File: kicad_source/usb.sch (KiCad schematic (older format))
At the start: 19 parts, among them P1 USB_OTG, Q3 BC847, Q4 BC847, U4 CP2102N_28

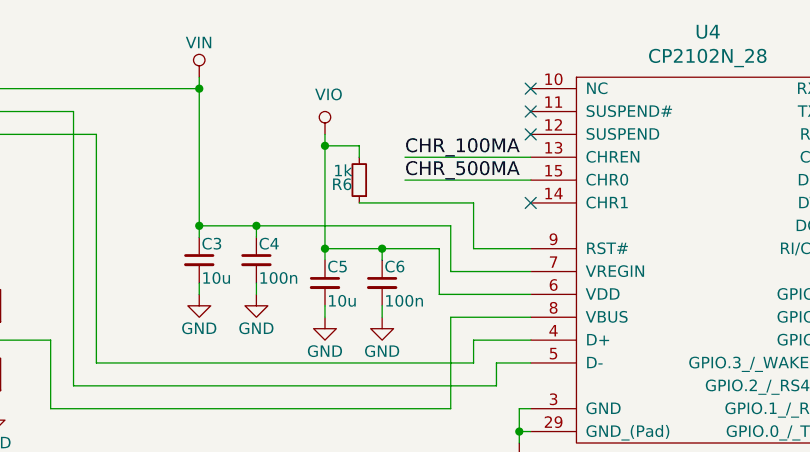
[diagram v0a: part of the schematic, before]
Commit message: updated power circuit
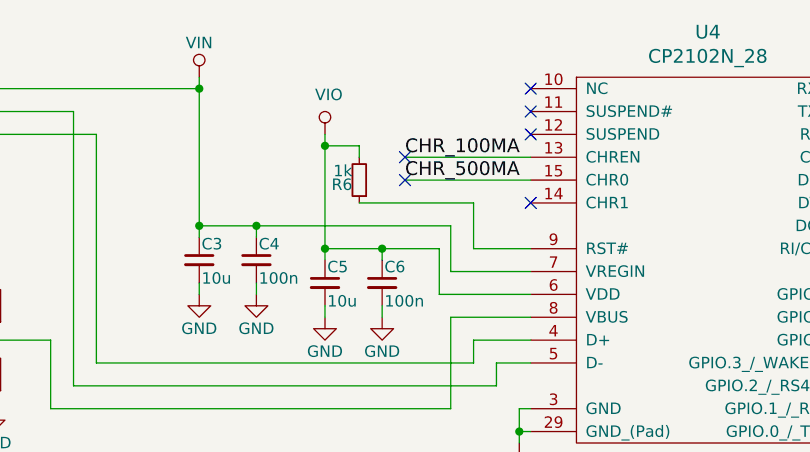
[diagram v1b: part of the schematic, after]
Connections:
- no-connect marks 13 -> 15
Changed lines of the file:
@@
 Text GLabel 10550 4050 2    60   Output ~ 0
 BOOT
+NoConn ~ 5000 2150
+NoConn ~ 5000 2250
 $EndSCHEMATC

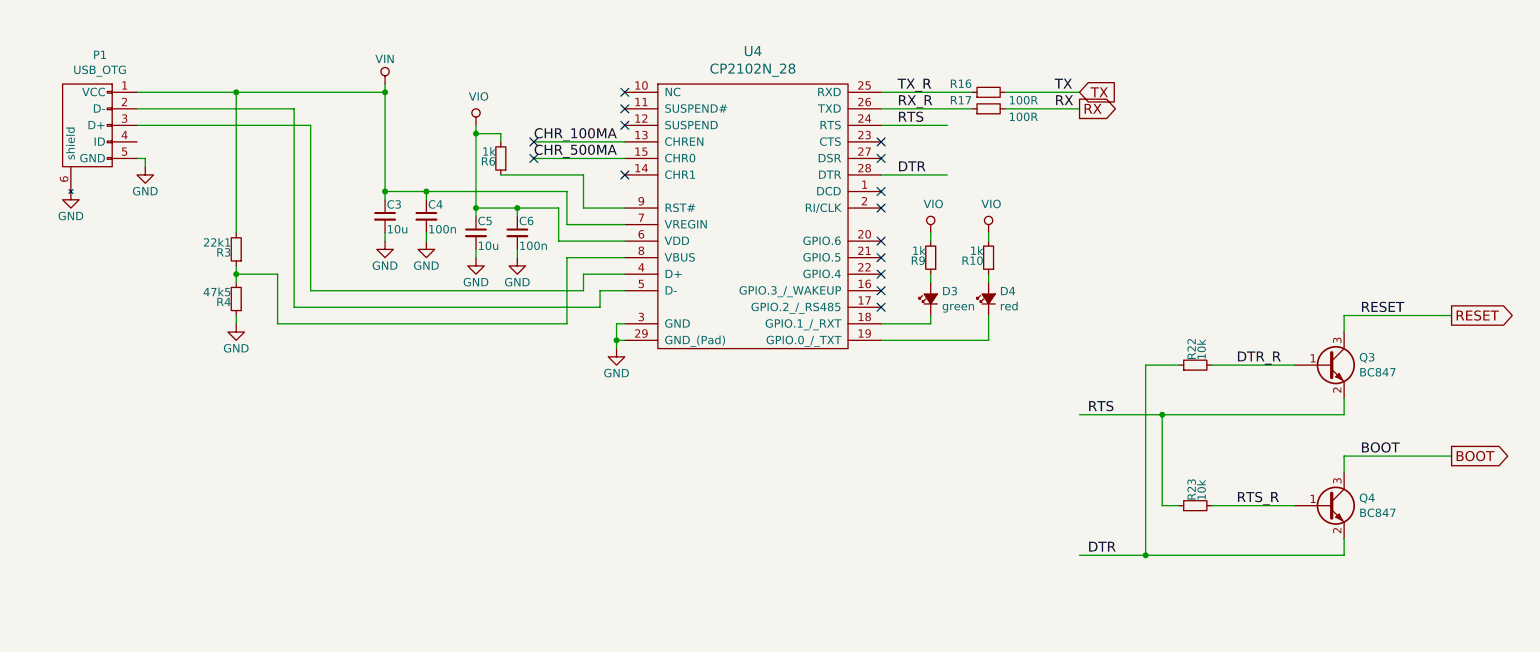
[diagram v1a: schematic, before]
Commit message: added flash, JTAG connector and display to schematic
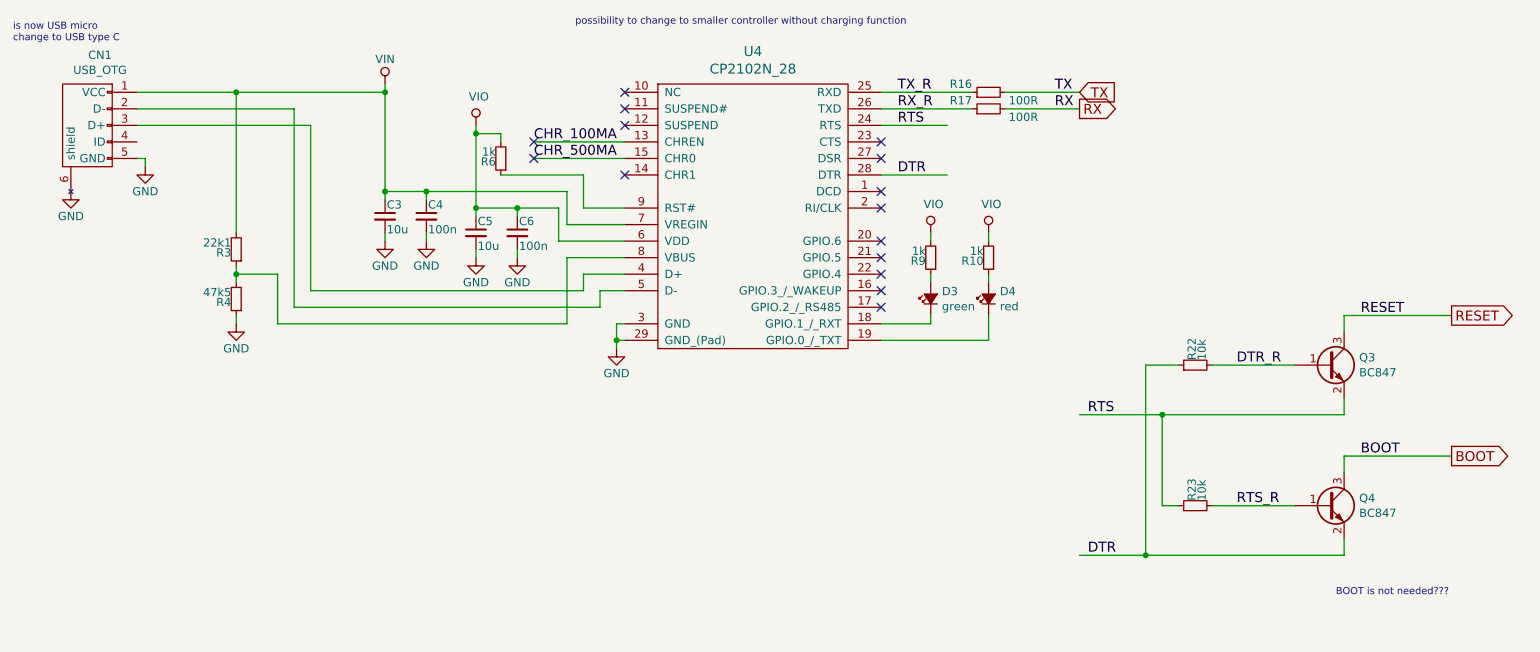
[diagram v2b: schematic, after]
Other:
- note added: "BOOT is not needed???"
- note added: "is now USB micro\nchange to USB type C"
- note added: "possibility to change to smaller controller without charging function"
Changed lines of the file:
@@
 AR Path="/5CB4789B" Ref="P?"  Part="1"
 AR Path="/5CB34EF4/5CB4789B" Ref="P1"  Part="1"
-AR Path="/5EB35E34/5CB4789B" Ref="P1"  Part="1"
-F 0 "P1" V 1875 1974 50  0000 C CNN
+AR Path="/5EB35E34/5CB4789B" Ref="CN1"  Part="1"
+F 0 "CN1" V 1875 1974 50  0000 C CNN
 F 1 "USB_OTG" V 1966 1974 50  0000 C CNN
 F 2 "CON_wuerth:WE_629105136821" V 2250 1950 50  0001 C CNN
@@
 NoConn ~ 5000 2150
 NoConn ~ 5000 2250
+Text Notes 9850 4900 0    43   ~ 0
+BOOT is not needed???
+Text Notes 5250 1450 0    43   ~ 0
+possibility to change to smaller controller without charging function
+Text Notes 1850 1550 0    43   ~ 0
+is now USB micro\nchange to USB type C
 $EndSCHEMATC

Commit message: added nfc part, generated schematic pdf
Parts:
- renumbered C3 to C28, C4 to C29, C5 to C30, C6 to C31, D3 to D5, D4 to D6, Q3 to Q2, Q4 to Q3, R3 to R18, R4 to R19, R6 to R20, R9 to R21, R16 to R22, R17 to R23, R10 to R24, R22 to R25, R23 to R26

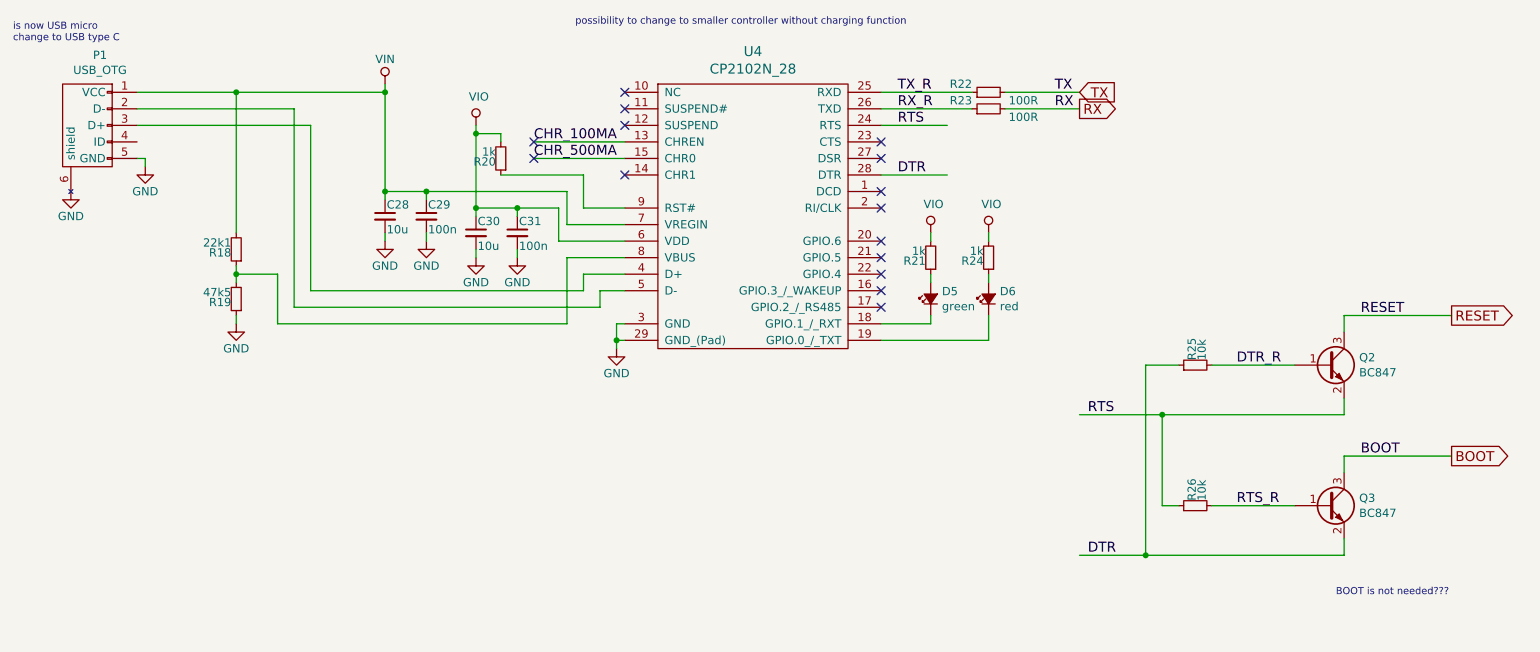
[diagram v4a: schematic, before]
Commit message: changed usb controller to FTDI FT230XS
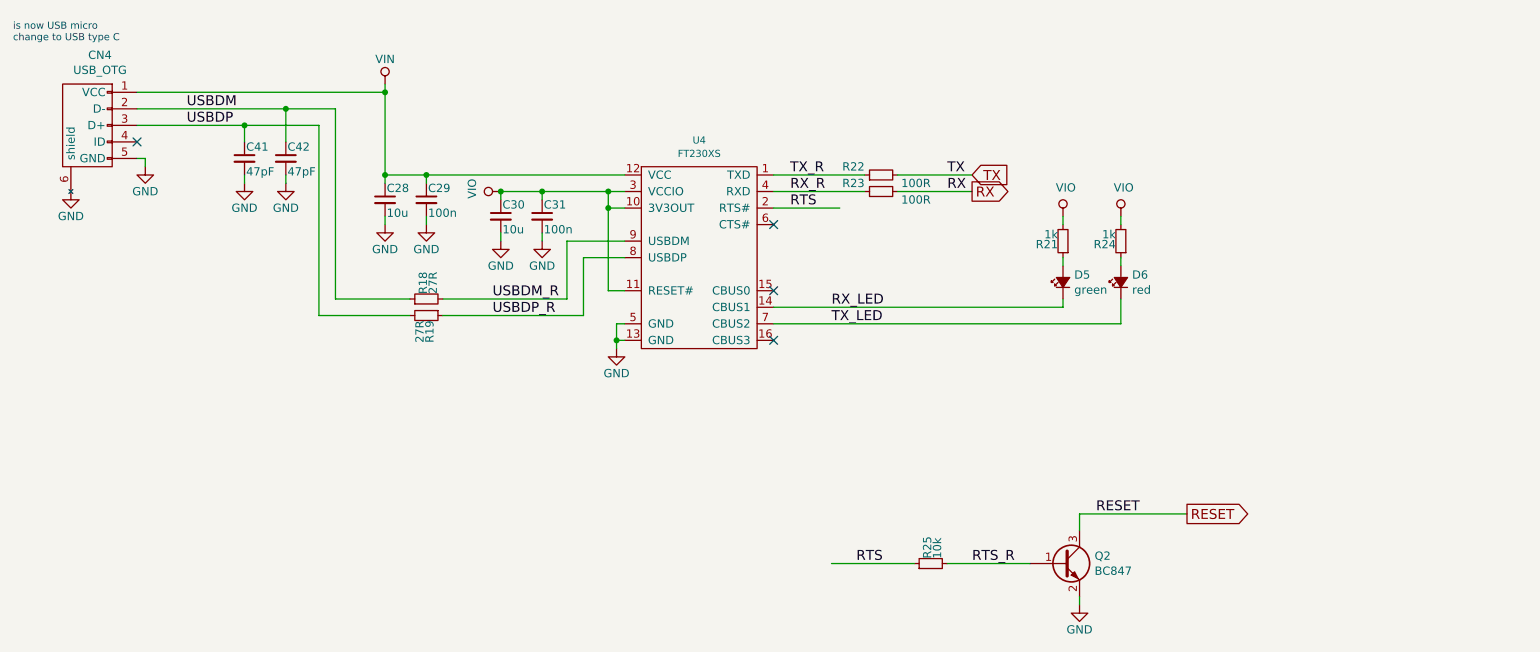
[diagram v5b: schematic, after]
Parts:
- removed Q3: BC847, SOT_TO:SOT-23, symbol devices:Q_NPN_BEC
- removed R20: 1k, resistors:R_0603, symbol devices:R_1206
- removed R26: 10k, resistors:R_0603, symbol devices:R_1206
- removed U4: CP2102N_28, QFN:QFN-28-1EP_5x5mm_Pitch0.5mm, symbol IC_interface_usb:CP2102N_28
- added C41, C42: 47pF, capacitors:C_0603, symbol devices:C_0603
- added U4: FT230XS, SSOP:SSOP-16_3.9x4.9mm_Pitch0.635mm, symbol IC_interface_usb:FT230XS
- R18: value 22k1 -> 27R
- R19: value 47k5 -> 27R
- renumbered P1 to CN4
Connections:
- net labels added: RX_LED, TX_LED, USBDM, USBDM_R, USBDP, USBDP_R
- net labels removed: BOOT, CHR_100MA, CHR_500MA, DTR, DTR_R
- wire segments 84 -> 62
- no-connect marks 15 -> 4
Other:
- note removed: "BOOT is not needed???"
- note removed: "possibility to change to smaller controller without charging function"
- moved on the sheet: C28, C29, C30, C31, D5, D6, Q2, R18, R19, R21, R22, R23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

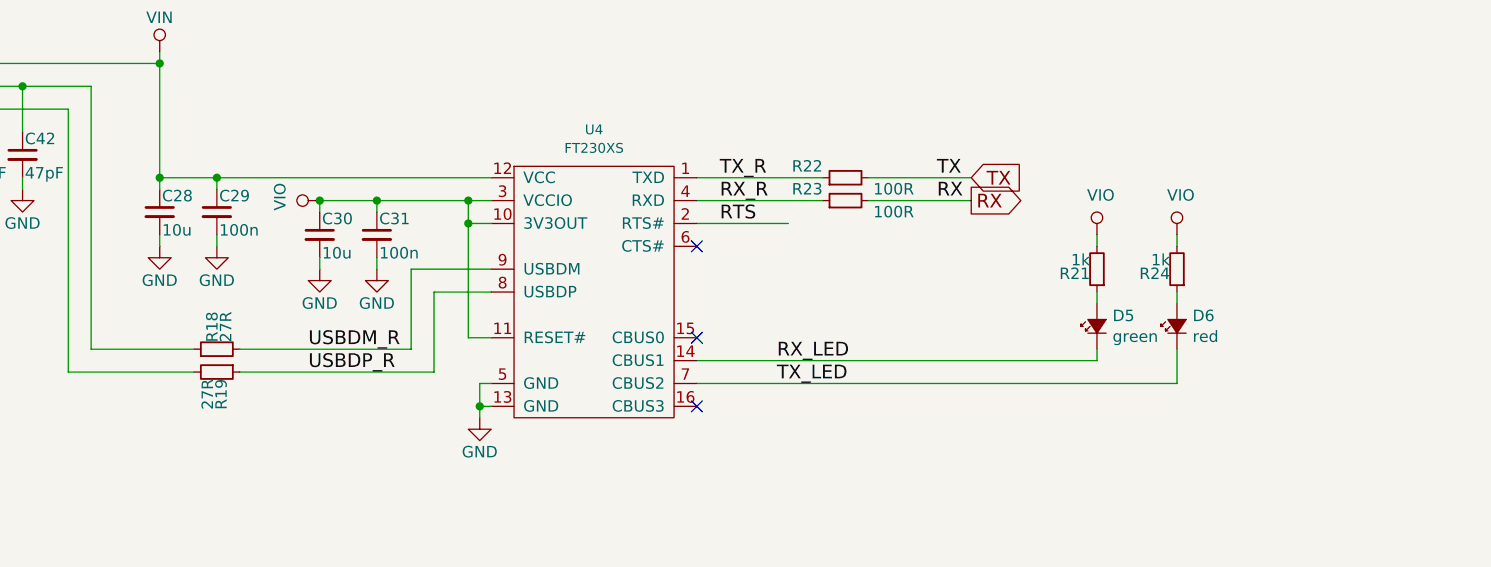
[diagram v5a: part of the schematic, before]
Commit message: corrected some part numbers
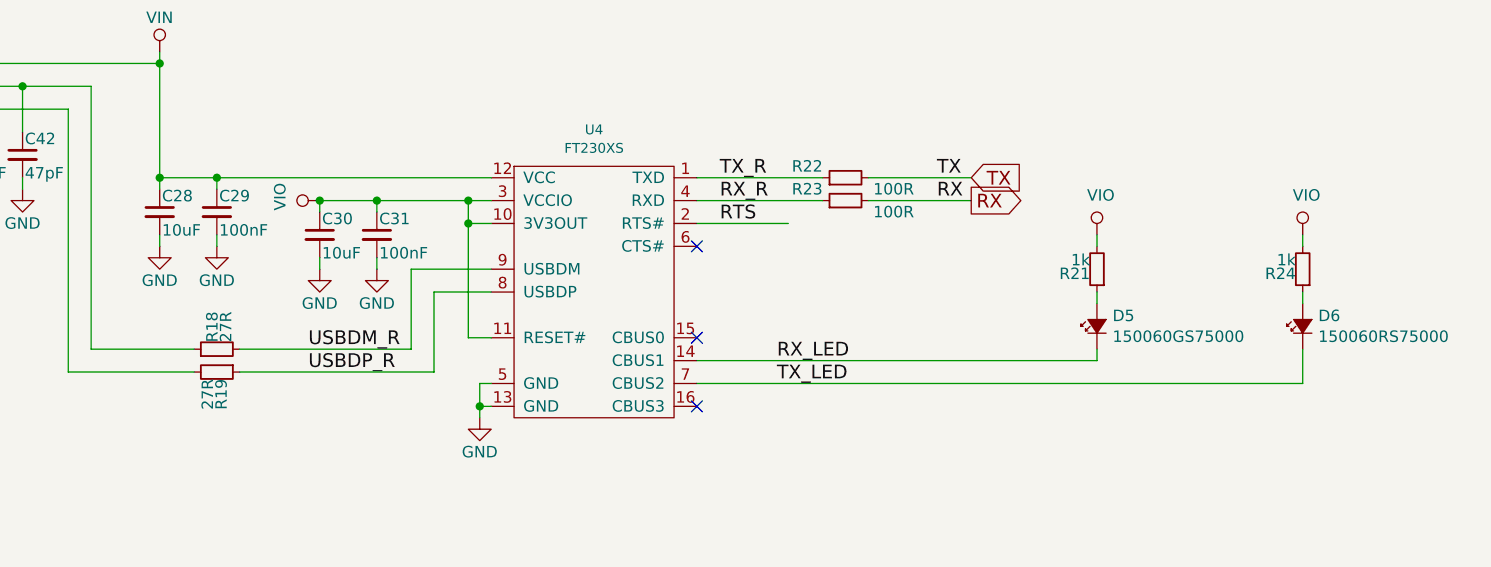
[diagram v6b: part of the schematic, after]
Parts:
- C28, C30: value 10u -> 10uF
- C29, C31: value 100n -> 100nF
- D5: value green -> 150060GS75000
- D6: value red -> 150060RS75000
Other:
- moved on the sheet: D6, R24
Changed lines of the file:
@@
 AR Path="/5EB35E34/5CB478B7" Ref="C28"  Part="1"
 F 0 "C28" H 4110 2570 50  0000 L CNN
-F 1 "10u" H 4110 2420 50  0000 L CNN
+F 1 "10uF" H 4110 2420 50  0000 L CNN
 F 2 "capacitors:C_0603" H 4100 2350 50  0001 C CNN
 F 3 "" H 4100 2500 50  0000 C CNN
@@
 AR Path="/5EB35E34/5CB478BE" Ref="C29"  Part="1"
 F 0 "C29" H 4360 2570 50  0000 L CNN
-F 1 "100n" H 4360 2420 50  0000 L CNN
+F 1 "100nF" H 4360 2420 50  0000 L CNN
 F 2 "capacitors:C_0603" H 4350 2350 50  0001 C CNN
 F 3 "" H 4350 2500 50  0000 C CNN
@@
 AR Path="/5EB35E34/5CB478D4" Ref="C31"  Part="1"
 F 0 "C31" H 5060 2670 50  0000 L CNN
-F 1 "100n" H 5060 2520 50  0000 L CNN
+F 1 "100nF" H 5060 2520 50  0000 L CNN
 F 2 "capacitors:C_0603" H 5050 2450 50  0001 C CNN
 F 3 "" H 5050 2600 50  0000 C CNN
@@
 AR Path="/5EB35E34/5CB478DB" Ref="C30"  Part="1"
 F 0 "C30" H 4810 2670 50  0000 L CNN
-F 1 "10u" H 4810 2520 50  0000 L CNN
+F 1 "10uF" H 4810 2520 50  0000 L CNN
 F 2 "capacitors:C_0603" H 4800 2450 50  0001 C CNN
 F 3 "" H 4800 2600 50  0000 C CNN
@@
 AR Path="/5EB35E34/5CB4794B" Ref="D5"  Part="1"
 F 0 "D5" V 8246 2932 50  0000 R CNN
-F 1 "green" V 8155 2932 50  0000 R CNN
+F 1 "150060GS75000" V 8155 2932 50  0000 R CNN
 F 2 "LEDs:LED_0603" V 8200 3000 50  0001 C CNN
 F 3 "" V 8200 3000 50  0000 C CNN
@@
 L devices:Led_Small D?
 U 1 1 5CB47952
-P 8550 3000
+P 9100 3000
 AR Path="/5CB47952" Ref="D?"  Part="1"
 AR Path="/5CB34EF4/5CB47952" Ref="D?"  Part="1"
 AR Path="/5EB35E34/5CB47952" Ref="D6"  Part="1"
-F 0 "D6" V 8596 2932 50  0000 R CNN
-F 1 "red" V 8505 2932 50  0000 R CNN
-F 2 "LEDs:LED_0603" V 8550 3000 50  0001 C CNN
-F 3 "" V 8550 3000 50  0000 C CNN
-	1    8550 3000
+F 0 "D6" V 9146 2932 50  0000 R CNN
+F 1 "150060RS75000" V 9055 2932 50  0000 R CNN
+F 2 "LEDs:LED_0603" V 9100 3000 50  0001 C CNN
+F 3 "" V 9100 3000 50  0000 C CNN
+	1    9100 3000
 	0    -1   -1   0
 $EndComp
@@
 L devices:R_1206 R?
 U 1 1 5CB47960
-P 8550 2750
+P 9100 2750
 AR Path="/5CB47960" Ref="R?"  Part="1"
 AR Path="/5CB34EF4/5CB47960" Ref="R?"  Part="1"
 AR Path="/5EB35E34/5CB47960" Ref="R24"  Part="1"
-F 0 "R24" H 8580 2770 50  0000 L CNN
-F 1 "1k" H 8580 2710 50  0000 L CNN
-F 2 "resistors:R_0603" H 8550 2600 50  0001 C CNN
-F 3 "" H 8550 2750 50  0000 C CNN
-	1    8550 2750
+F 0 "R24" H 9130 2770 50  0000 L CNN
+F 1 "1k" H 9130 2710 50  0000 L CNN
+F 2 "resistors:R_0603" H 9100 2600 50  0001 C CNN
+F 3 "" H 9100 2750 50  0000 C CNN
+	1    9100 2750
 	-1   0    0    1
 $EndComp
@@
 L power-supply:VIO #PWR?
 U 1 1 5CB4797D
-P 8550 2600
+P 9100 2600
 AR Path="/5CB4797D" Ref="#PWR?"  Part="1"
 AR Path="/5CB34EF4/5CB4797D" Ref="#PWR?"  Part="1"
 AR Path="/5EB35E34/5CB4797D" Ref="#PWR065"  Part="1"
-F 0 "#PWR065" H 8550 2450 50  0001 C CNN
-F 1 "VIO" H 8567 2773 50  0000 C CNN
-F 2 "" H 8550 2600 50  0000 C CNN
-F 3 "" H 8550 2600 50  0000 C CNN
-	1    8550 2600
+F 0 "#PWR065" H 9100 2450 50  0001 C CNN
+F 1 "VIO" H 9117 2773 50  0000 C CNN
+F 2 "" H 9100 2600 50  0000 C CNN
+F 3 "" H 9100 2600 50  0000 C CNN
+	1    9100 2600
 	1    0    0    -1
 $EndComp
@@
 	8200 2600 8200 2650
 Wire Wire Line
-	8550 2600 8550 2650
+	9100 2600 9100 2650
 Wire Wire Line
 	8200 2850 8200 2900
 Wire Wire Line
-	8550 2850 8550 2900
+	9100 2850 9100 2900
 Wire Wire Line
 	8200 3100 8200 3150
-Wire Wire Line
-	8550 3100 8550 3250
 Wire Wire Line
 	7000 2350 6450 2350
@@
 Wire Wire Line
 	6450 3150 8200 3150
-Wire Wire Line
-	6450 3250 8550 3250
 Text Label 6800 3150 0    60   ~ 0
 RX_LED
@@
 Wire Wire Line
 	8300 4900 8300 4950
+Wire Wire Line
+	9100 3250 9100 3100
+Wire Wire Line
+	6450 3250 9100 3250
 $EndSCHEMATC

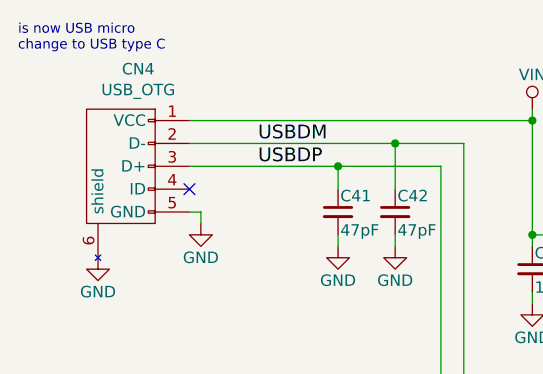
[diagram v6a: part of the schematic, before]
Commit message: optimized parts for BOM costs
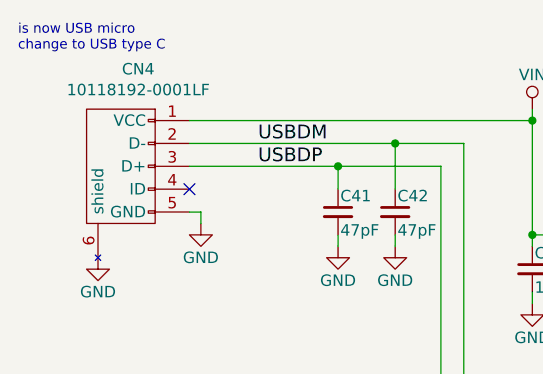
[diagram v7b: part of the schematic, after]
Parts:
- CN4: value USB_OTG -> 10118192-0001LF; footprint CON_wuerth:WE_629105136821 -> CON_wuerth:10118192-000xLF
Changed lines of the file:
@@
 AR Path="/5EB35E34/5CB4789B" Ref="CN4"  Part="1"
 F 0 "CN4" V 1875 1974 50  0000 C CNN
-F 1 "USB_OTG" V 1966 1974 50  0000 C CNN
-F 2 "CON_wuerth:WE_629105136821" V 2250 1950 50  0001 C CNN
+F 1 "10118192-0001LF" V 1966 1974 50  0000 C CNN
+F 2 "CON_wuerth:10118192-000xLF" V 2250 1950 50  0001 C CNN
 F 3 "" V 2250 1950 50  0000 C CNN
 	1    2300 2050
